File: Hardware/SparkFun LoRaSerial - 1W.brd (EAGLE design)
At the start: 50.8 x 27.9 mm, 75 parts, among them J1 QWIIC_RIGHT_ANGLE, J3 USB C, J4 JTAG, U2 ATSAMD21G-A, U3 AP2112K-3.3, U4 E19-915M30S, Y1 32.768kHz

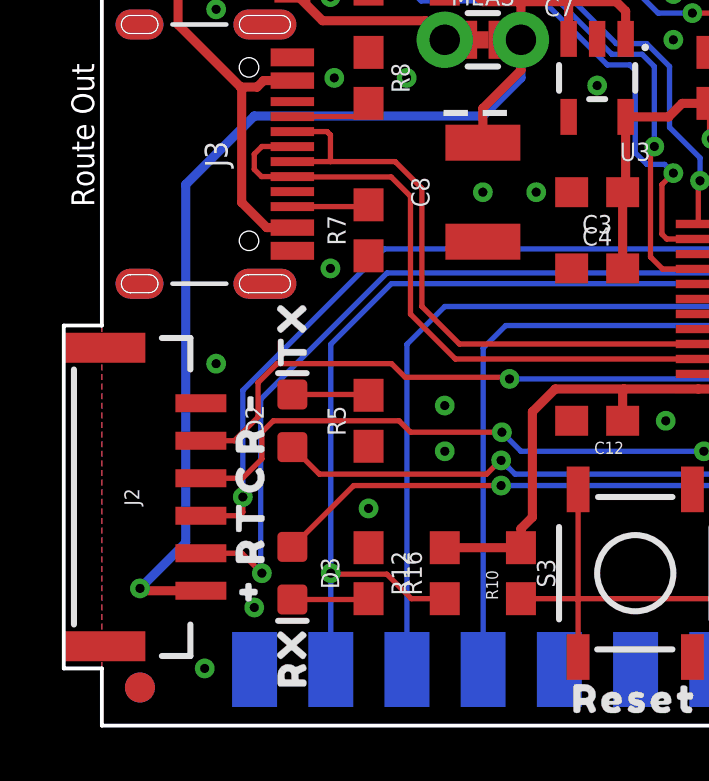
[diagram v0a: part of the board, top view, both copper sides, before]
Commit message: Fix reversed pinout on locking JST.
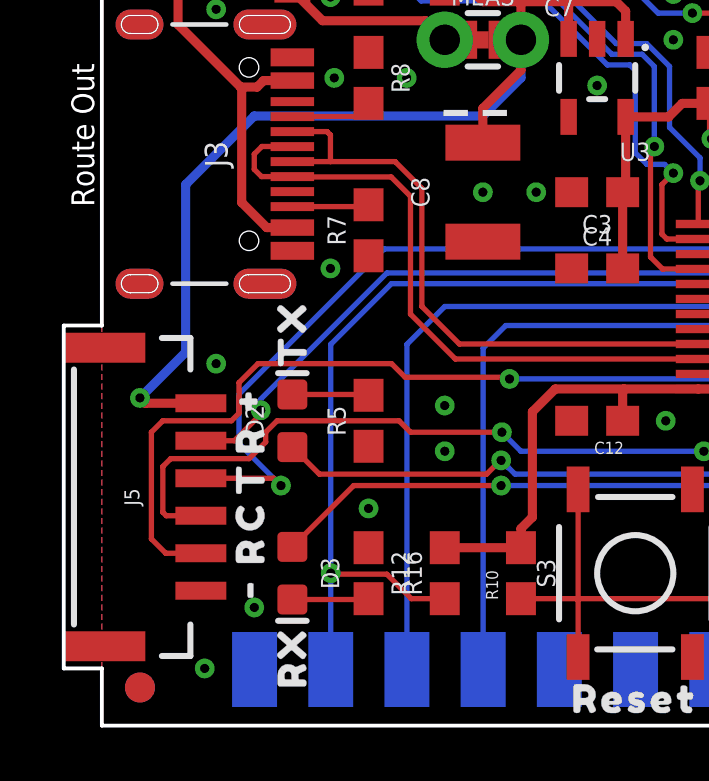
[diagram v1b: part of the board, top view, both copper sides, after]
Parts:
- moved U$12 6.35 mm to (6.22, 10.8)
- moved U$13 6.22 mm to (6.22, 4.57)
- moved U$15 1.27 mm to (6.22, 8.26)
- moved U$16 1.27 mm to (6.22, 6.99)
- renumbered J2 to J5
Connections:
- net 5V: now also J5.1; no longer J5.6
- net D30/CTS-I: now also J5.4; no longer J5.3
- net D38/RTS-O: now also J5.5; no longer J5.2
- net GND: now also J5.6; no longer J5.1
- net RX-I: now also J5.2; no longer J5.5
- net TX-O: now also J5.3; no longer J5.4
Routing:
- net D38/RTS-O: track 28.1 -> 35.0 mm
- net 5V: track 51.6 -> 45.3 mm
- net RX-I: track 33.4 -> 28.1 mm
- net D30/CTS-I: track 20.1 -> 23.7 mm
- net TX-O: track 30.8 -> 31.9 mm
